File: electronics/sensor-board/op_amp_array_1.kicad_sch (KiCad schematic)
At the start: 1 part

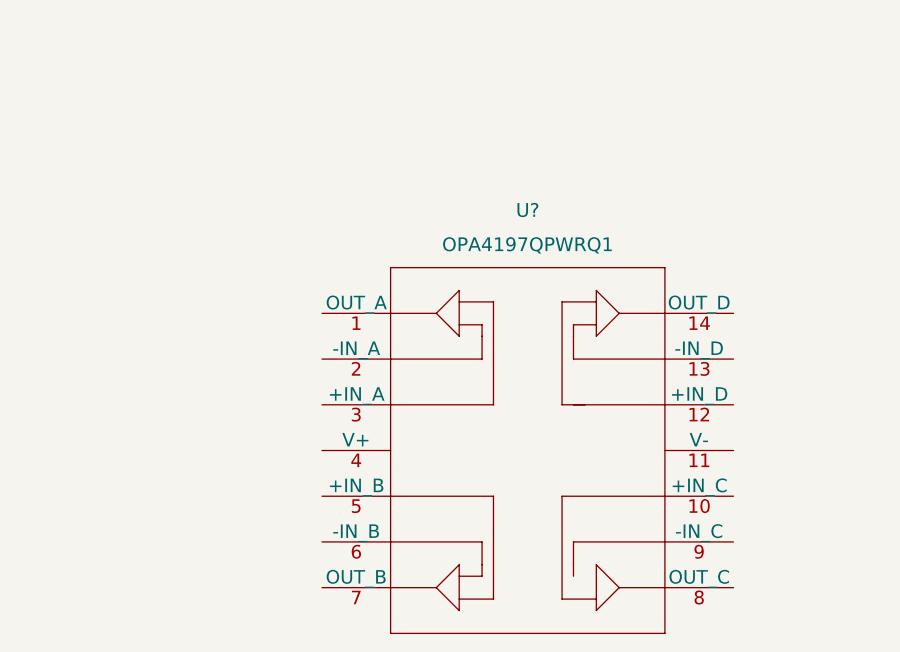
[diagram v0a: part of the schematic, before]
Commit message: Switched Op Amps
Added library files for both op amps (precision and general purpose)
Couldn't find symbol library for gen-purp. op amp
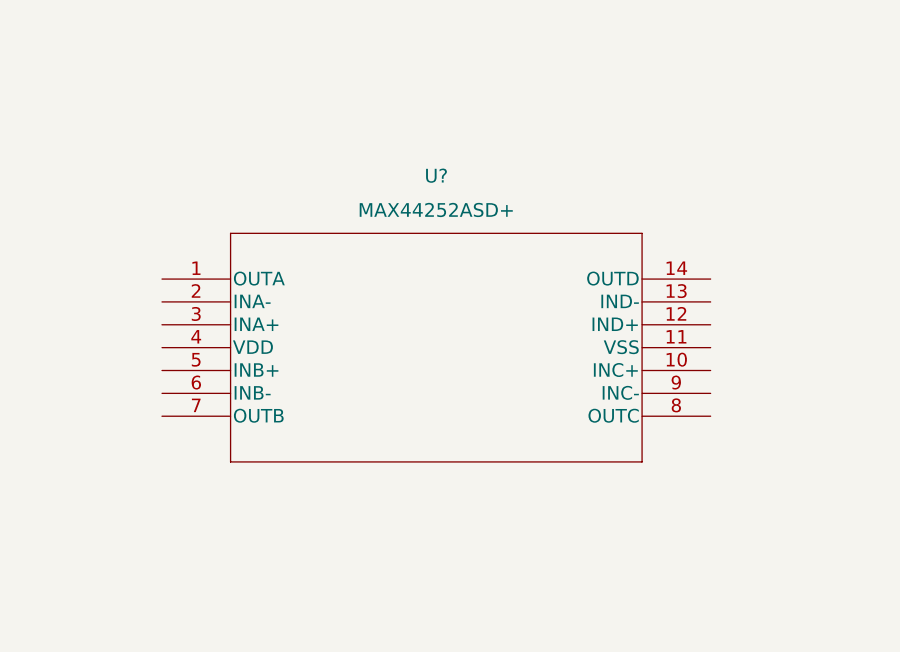
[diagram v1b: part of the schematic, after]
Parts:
- removed U?: OPA4197QPWRQ1, TSSOP_QPWRQ1_TEX, symbol OPA4197QPWRQ1:OPA4197QPWRQ1
- added U?: MAX44252ASD+, 21-0041B_14_MXM, symbol MAX44252ASD-:MAX44252ASD+
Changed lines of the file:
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@@
     (pin "1")
   )
-  (symbol (lib_id "OPA4197QPWRQ1:OPA4197QPWRQ1") (at 133.35 88.9 0) (unit 1)
+  (symbol (lib_id "MAX44252ASD-:MAX44252ASD+") (at 115.57 85.09 0) (unit 1)
     (in_bom yes) (on_board yes) (fields_autoplaced)
-    (property "Reference" "U?" (id 0) (at 156.21 77.47 0)
+    (property "Reference" "U?" (id 0) (at 146.05 73.66 0)
       (effects (font (size 1.524 1.524)))
     )
-    (property "Value" "OPA4197QPWRQ1" (id 1) (at 156.21 81.28 0)
+    (property "Value" "MAX44252ASD+" (id 1) (at 146.05 77.47 0)
       (effects (font (size 1.524 1.524)))
     )
-    (property "Footprint" "TSSOP_QPWRQ1_TEX" (id 2) (at 156.21 77.724 0)
+    (property "Footprint" "21-0041B_14_MXM" (id 2) (at 146.05 78.994 0)
       (effects (font (size 1.524 1.524)) hide)
     )
-    (property "Datasheet" "" (id 3) (at 133.35 88.9 0)
+    (property "Datasheet" "" (id 3) (at 115.57 85.09 0)
       (effects (font (size 1.524 1.524)))
     )

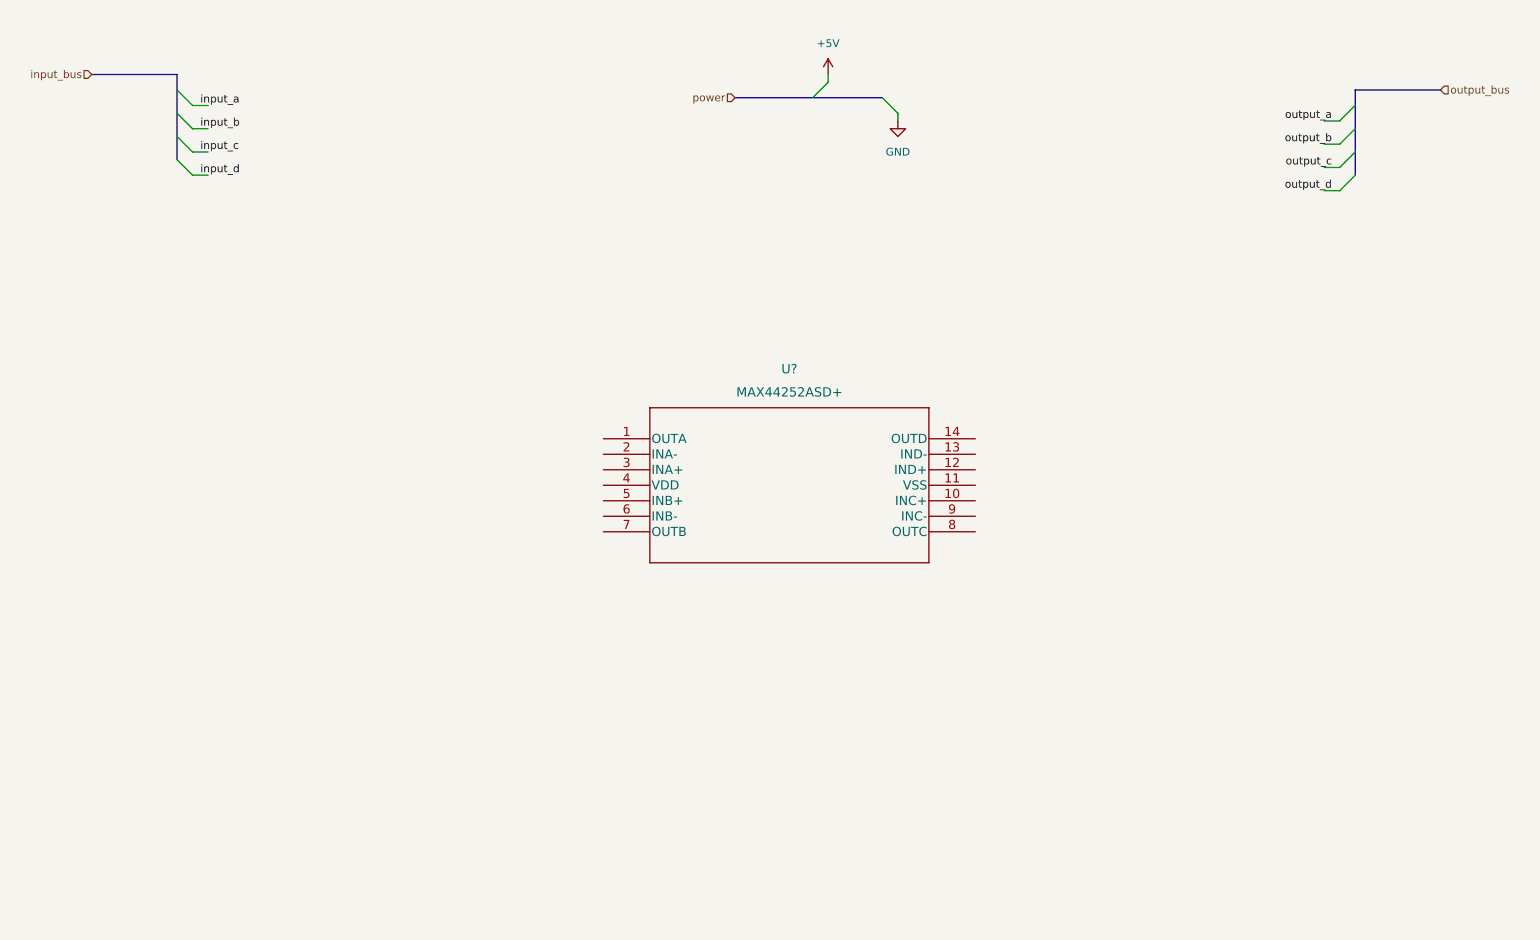
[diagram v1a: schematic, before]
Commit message: Custom MAX44252 symbol created
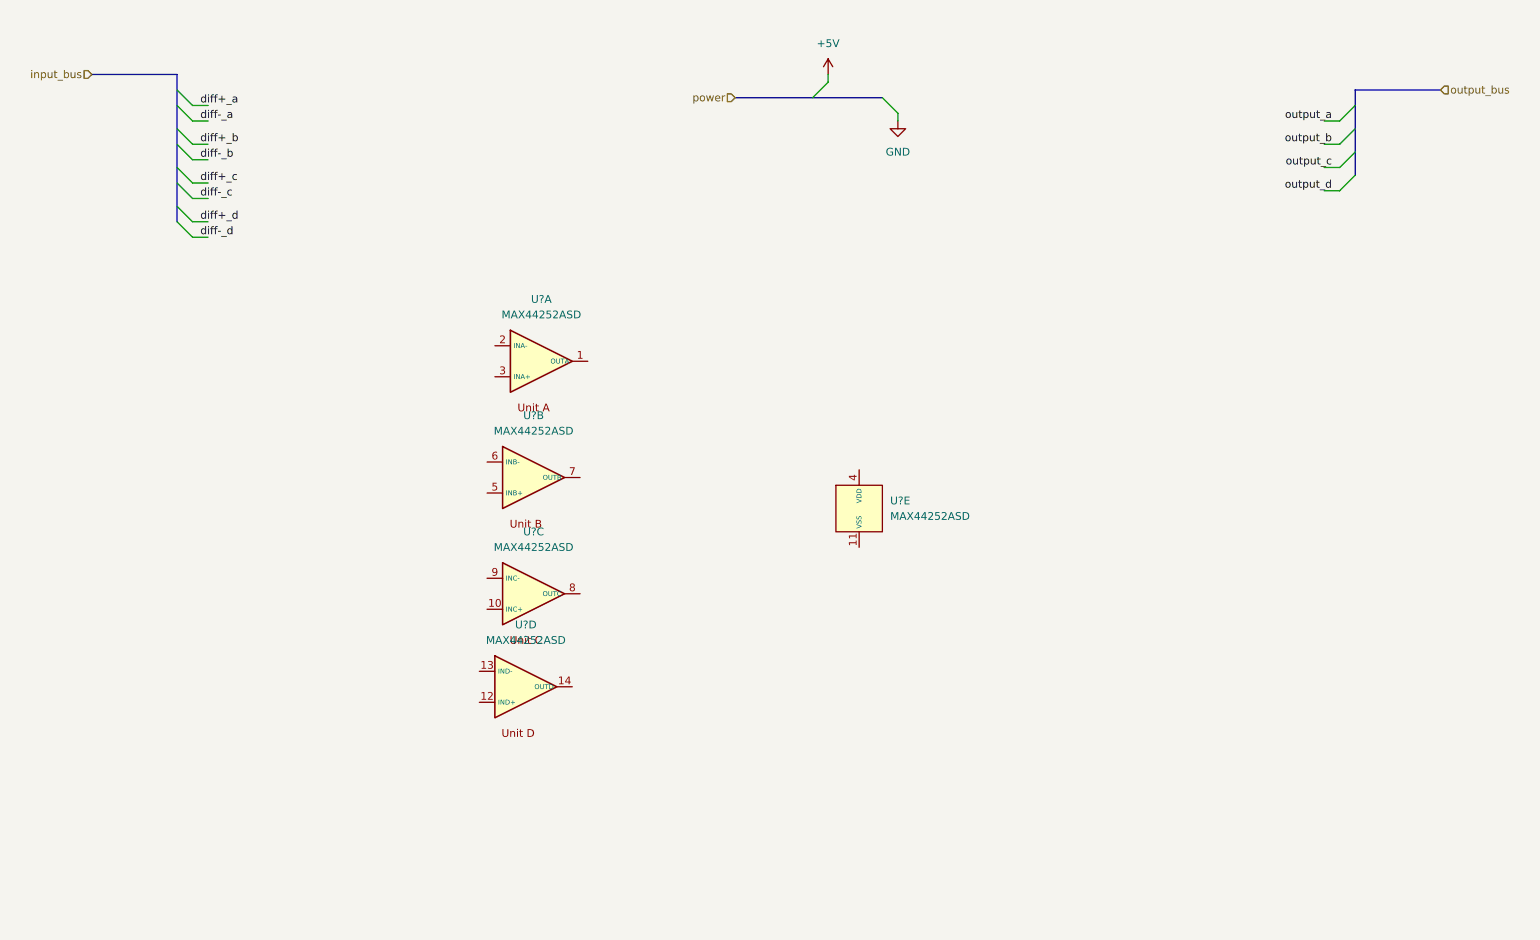
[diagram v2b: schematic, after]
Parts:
- removed U?: MAX44252ASD+, 21-0041B_14_MXM, symbol MAX44252ASD-:MAX44252ASD+
- added U? (x5): MAX44252ASD, symbol MAX44252ASD_Custom:MAX44252ASD
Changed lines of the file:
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@@
     (stroke (width 0) (type default) (color 0 0 0 0))
   )
-  (bus_entry (at 45.72 31.75) (size 2.54 2.54)
-    (stroke (width 0) (type default) (color 0 0 0 0))
-  )
-  (bus_entry (at 45.72 35.56) (size 2.54 2.54)
-    (stroke (width 0) (type default) (color 0 0 0 0))
-  )
-  (bus_entry (at 45.72 39.37) (size 2.54 2.54)
+  (bus_entry (at 45.72 30.48) (size 2.54 2.54)
+    (stroke (width 0) (type default) (color 0 0 0 0))
+  )
+  (bus_entry (at 45.72 34.29) (size 2.54 2.54)
+    (stroke (width 0) (type default) (color 0 0 0 0))
+  )
+  (bus_entry (at 45.72 36.83) (size 2.54 2.54)
+    (stroke (width 0) (type default) (color 0 0 0 0))
+  )
+  (bus_entry (at 45.72 40.64) (size 2.54 2.54)
+    (stroke (width 0) (type default) (color 0 0 0 0))
+  )
+  (bus_entry (at 45.72 43.18) (size 2.54 2.54)
+    (stroke (width 0) (type default) (color 0 0 0 0))
+  )
+  (bus_entry (at 45.72 46.99) (size 2.54 2.54)
+    (stroke (width 0) (type default) (color 0 0 0 0))
+  )
+  (bus_entry (at 45.72 49.53) (size 2.54 2.54)
     (stroke (width 0) (type default) (color 0 0 0 0))
   )
@@
     (stroke (width 0) (type default) (color 0 0 0 0))
   )
-  (wire (pts (xy 48.26 34.29) (xy 50.8 34.29))
-    (stroke (width 0) (type default) (color 0 0 0 0))
-  )
-  (wire (pts (xy 48.26 38.1) (xy 50.8 38.1))
-    (stroke (width 0) (type default) (color 0 0 0 0))
-  )
-  (wire (pts (xy 48.26 41.91) (xy 50.8 41.91))
+  (wire (pts (xy 48.26 33.02) (xy 50.8 33.02))
+    (stroke (width 0) (type default) (color 0 0 0 0))
+  )
+  (wire (pts (xy 48.26 36.83) (xy 50.8 36.83))
+    (stroke (width 0) (type default) (color 0 0 0 0))
+  )
+  (wire (pts (xy 48.26 39.37) (xy 50.8 39.37))
+    (stroke (width 0) (type default) (color 0 0 0 0))
+  )
+  (wire (pts (xy 48.26 43.18) (xy 50.8 43.18))
+    (stroke (width 0) (type default) (color 0 0 0 0))
+  )
+  (wire (pts (xy 48.26 45.72) (xy 50.8 45.72))
+    (stroke (width 0) (type default) (color 0 0 0 0))
+  )
+  (wire (pts (xy 48.26 49.53) (xy 50.8 49.53))
+    (stroke (width 0) (type default) (color 0 0 0 0))
+  )
+  (wire (pts (xy 48.26 52.07) (xy 50.8 52.07))
     (stroke (width 0) (type default) (color 0 0 0 0))
   )
@@
     (stroke (width 0) (type default) (color 0 0 0 0))
   )
-  (bus (pts (xy 45.72 25.4) (xy 45.72 39.37))
+  (bus (pts (xy 45.72 25.4) (xy 45.72 49.53))
     (stroke (width 0) (type default) (color 0 0 0 0))
   )
@@
     (stroke (width 0) (type default) (color 0 0 0 0))
   )
-  (label "input_a" (at 49.53 30.48 0)
-    (effects (font (size 1.27 1.27)) (justify left bottom))
-  )
-  (label "input_b" (at 49.53 34.29 0)
-    (effects (font (size 1.27 1.27)) (justify left bottom))
-  )
-  (label "input_c" (at 49.53 38.1 0)
-    (effects (font (size 1.27 1.27)) (justify left bottom))
-  )
-  (label "input_d" (at 49.53 41.91 0)
+  (label "diff+_a" (at 49.53 30.48 0)
+    (effects (font (size 1.27 1.27)) (justify left bottom))
+  )
+  (label "diff-_a" (at 49.53 33.02 0)
+    (effects (font (size 1.27 1.27)) (justify left bottom))
+  )
+  (label "diff+_b" (at 49.53 36.83 0)
+    (effects (font (size 1.27 1.27)) (justify left bottom))
+  )
+  (label "diff-_b" (at 49.53 39.37 0)
+    (effects (font (size 1.27 1.27)) (justify left bottom))
+  )
+  (label "diff+_c" (at 49.53 43.18 0)
+    (effects (font (size 1.27 1.27)) (justify left bottom))
+  )
+  (label "diff-_c" (at 49.53 45.72 0)
+    (effects (font (size 1.27 1.27)) (justify left bottom))
+  )
+  (label "diff+_d" (at 49.53 49.53 0)
+    (effects (font (size 1.27 1.27)) (justify left bottom))
+  )
+  (label "diff-_d" (at 49.53 52.07 0)
     (effects (font (size 1.27 1.27)) (justify left bottom))
   )
@@
     (pin "1")
   )
-  (symbol (lib_id "MAX44252ASD-:MAX44252ASD+") (at 115.57 85.09 0) (unit 1)
-    (in_bom yes) (on_board yes) (fields_autoplaced)
-    (property "Reference" "U?" (id 0) (at 146.05 73.66 0)
-      (effects (font (size 1.524 1.524)))
-    )
-    (property "Value" "MAX44252ASD+" (id 1) (at 146.05 77.47 0)
-      (effects (font (size 1.524 1.524)))
-    )
-    (property "Footprint" "21-0041B_14_MXM" (id 2) (at 146.05 78.994 0)
-      (effects (font (size 1.524 1.524)) hide)
-    )
-    (property "Datasheet" "" (id 3) (at 115.57 85.09 0)
-      (effects (font (size 1.524 1.524)))
-    )
-    (pin "1")
-    (pin "10")
+  (symbol (lib_id "MAX44252ASD_Custom:MAX44252ASD") (at 157.48 96.52 0) (unit 5)
+    (in_bom yes) (on_board yes) (fields_autoplaced)
+    (property "Reference" "U?" (id 0) (at 162.56 95.2499 0)
+      (effects (font (size 1.27 1.27)) (justify left))
+    )
+    (property "Value" "MAX44252ASD" (id 1) (at 162.56 97.7899 0)
+      (effects (font (size 1.27 1.27)) (justify left))
+    )
+    (property "Footprint" "" (id 2) (at 159.385 96.52 0)
+      (effects (font (size 1.27 1.27)) hide)
+    )
+    (property "Datasheet" "" (id 3) (at 159.385 96.52 0)
+      (effects (font (size 1.27 1.27)) hide)
+    )
     (pin "11")
+    (pin "4")
+  )
+  (symbol (lib_id "MAX44252ASD_Custom:MAX44252ASD") (at 101.6 125.73 0) (unit 4)
+    (in_bom yes) (on_board yes) (fields_autoplaced)
+    (property "Reference" "U?" (id 0) (at 102.87 115.57 0))
+    (property "Value" "MAX44252ASD" (id 1) (at 102.87 118.11 0))
+    (property "Footprint" "" (id 2) (at 103.505 125.73 0)
+      (effects (font (size 1.27 1.27)) hide)
+    )
+    (property "Datasheet" "" (id 3) (at 103.505 125.73 0)
+      (effects (font (size 1.27 1.27)) hide)
+    )
     (pin "12")
     (pin "13")
     (pin "14")
-    (pin "2")
-    (pin "3")
-    (pin "4")
+  )
+  (symbol (lib_id "MAX44252ASD_Custom:MAX44252ASD") (at 102.87 91.44 0) (unit 2)
+    (in_bom yes) (on_board yes) (fields_autoplaced)
+    (property "Reference" "U?" (id 0) (at 104.14 81.28 0))
+    (property "Value" "MAX44252ASD" (id 1) (at 104.14 83.82 0))
+    (property "Footprint" "" (id 2) (at 104.775 91.44 0)
+      (effects (font (size 1.27 1.27)) hide)
+    )
+    (property "Datasheet" "" (id 3) (at 104.775 91.44 0)
+      (effects (font (size 1.27 1.27)) hide)
+    )
     (pin "5")
     (pin "6")
     (pin "7")
+  )
+  (symbol (lib_id "MAX44252ASD_Custom:MAX44252ASD") (at 102.87 110.49 0) (unit 3)
+    (in_bom yes) (on_board yes) (fields_autoplaced)
+    (property "Reference" "U?" (id 0) (at 104.14 100.33 0))
+    (property "Value" "MAX44252ASD" (id 1) (at 104.14 102.87 0))
+    (property "Footprint" "" (id 2) (at 104.775 110.49 0)
+      (effects (font (size 1.27 1.27)) hide)
+    )
+    (property "Datasheet" "" (id 3) (at 104.775 110.49 0)
+      (effects (font (size 1.27 1.27)) hide)
+    )
+    (pin "10")
     (pin "8")
     (pin "9")
   )
+  (symbol (lib_id "MAX44252ASD_Custom:MAX44252ASD") (at 104.14 72.39 0) (unit 1)
+    (in_bom yes) (on_board yes) (fields_autoplaced)
+    (property "Reference" "U?" (id 0) (at 105.41 62.23 0))
+    (property "Value" "MAX44252ASD" (id 1) (at 105.41 64.77 0))
+    (property "Footprint" "" (id 2) (at 106.045 72.39 0)
+      (effects (font (size 1.27 1.27)) hide)
+    )
+    (property "Datasheet" "" (id 3) (at 106.045 72.39 0)
+      (effects (font (size 1.27 1.27)) hide)
+    )
+    (pin "1")
+    (pin "2")
+    (pin "3")
+  )
 )

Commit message: sensor-board edit, base differential amp. laid out
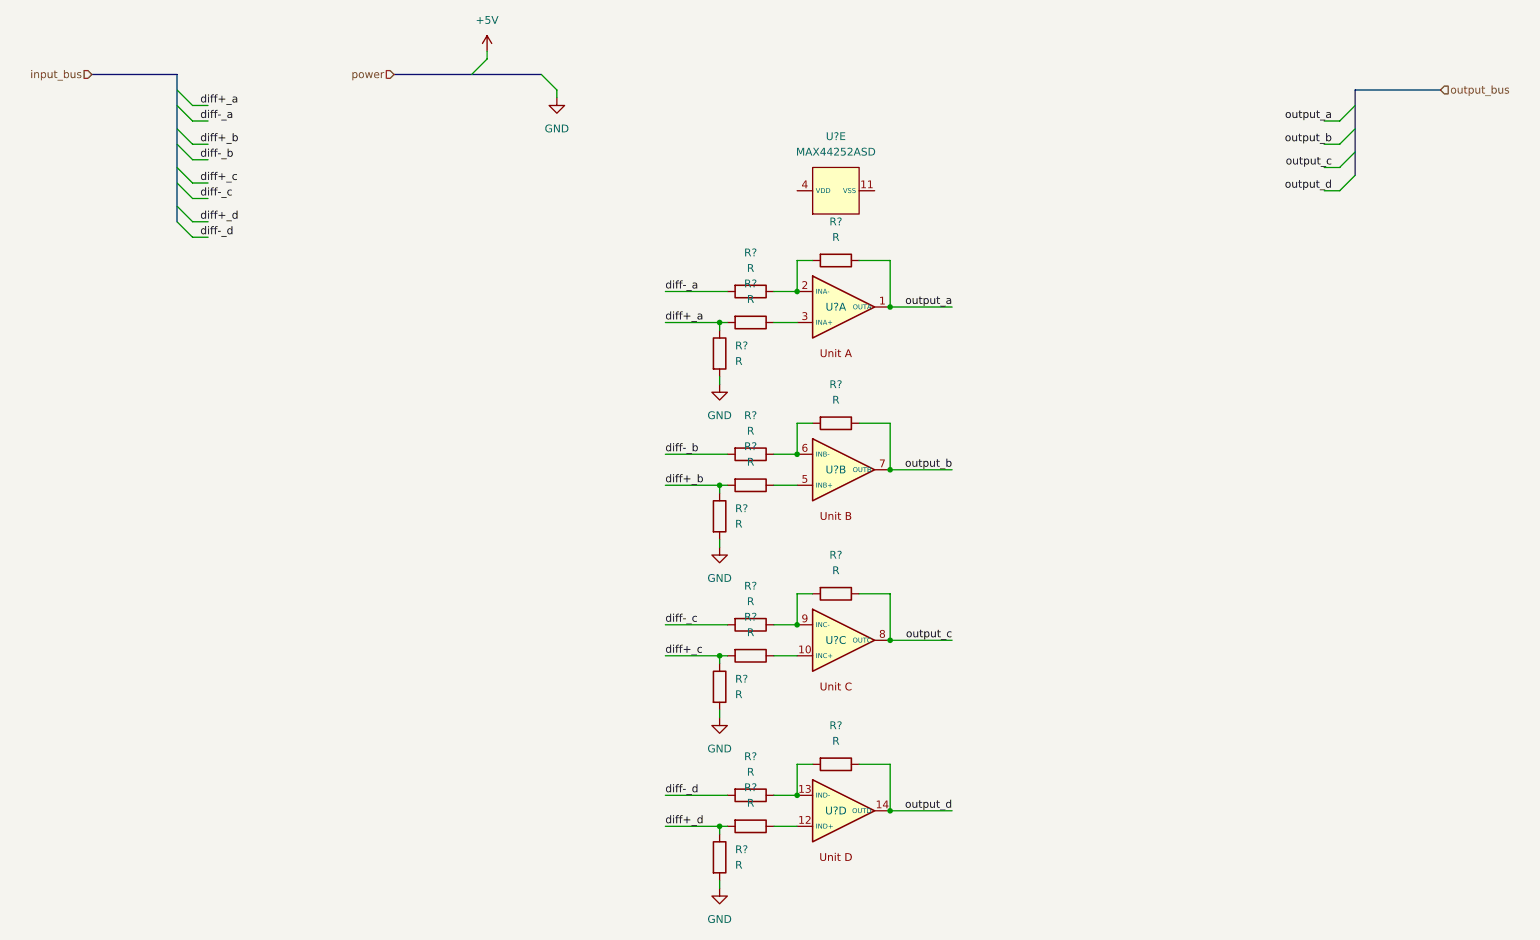
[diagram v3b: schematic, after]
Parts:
- added R? (x16): R, symbol Device:R
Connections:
- net GND: now also R?.2, R?.2, R?.2, R?.2
- net diff+_a: now also R?.1, R?.2
- net diff+_b: now also R?.1, R?.2
- net diff+_c: now also R?.1, R?.2
- net diff+_d: now also R?.1, R?.2
- net diff-_a: now also R?.2
- net diff-_b: now also R?.2
- net diff-_c: now also R?.2
- net diff-_d: now also R?.2
- net output_a: now also U?.1 (OUTA), R?.1
- net output_b: now also U?.7 (OUTB), R?.1
- net output_c: now also U?.8 (OUTC), R?.1
- net output_d: now also U?.14 (OUTD), R?.1
- net at U?.10 (INC+): now also R?.1
- net at U?.9 (INC-): now also R?.1, R?.2
- net at U?.5 (INB+): now also R?.1
- net at U?.6 (INB-): now also R?.1, R?.2
- net at U?.2 (INA-): now also R?.1, R?.2
- net at U?.3 (INA+): now also R?.1
- net at U?.12 (IND+): now also R?.1
- net at U?.13 (IND-): now also R?.1, R?.2
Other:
- moved on the sheet: U?A, U?B, U?C, U?D, U?E
